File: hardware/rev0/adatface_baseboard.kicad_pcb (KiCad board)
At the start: 4 copper layers, 121.3 x 111.6 mm, 90 parts, among them J1 Conn_01x06_Male, J2 Conn_02x32_Odd_Even, J3 Conn_02x32_Odd_Even, J4 Connector_USB_C_Receptacle_US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, J5 Connector_USB_C_Receptacle_US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, J6 Conn_01x06_Male, J7 Conn_01x26_Male, J8 Conn_01x01_Male, J9 Conn_01x01_Male, U1 PLR135_T8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

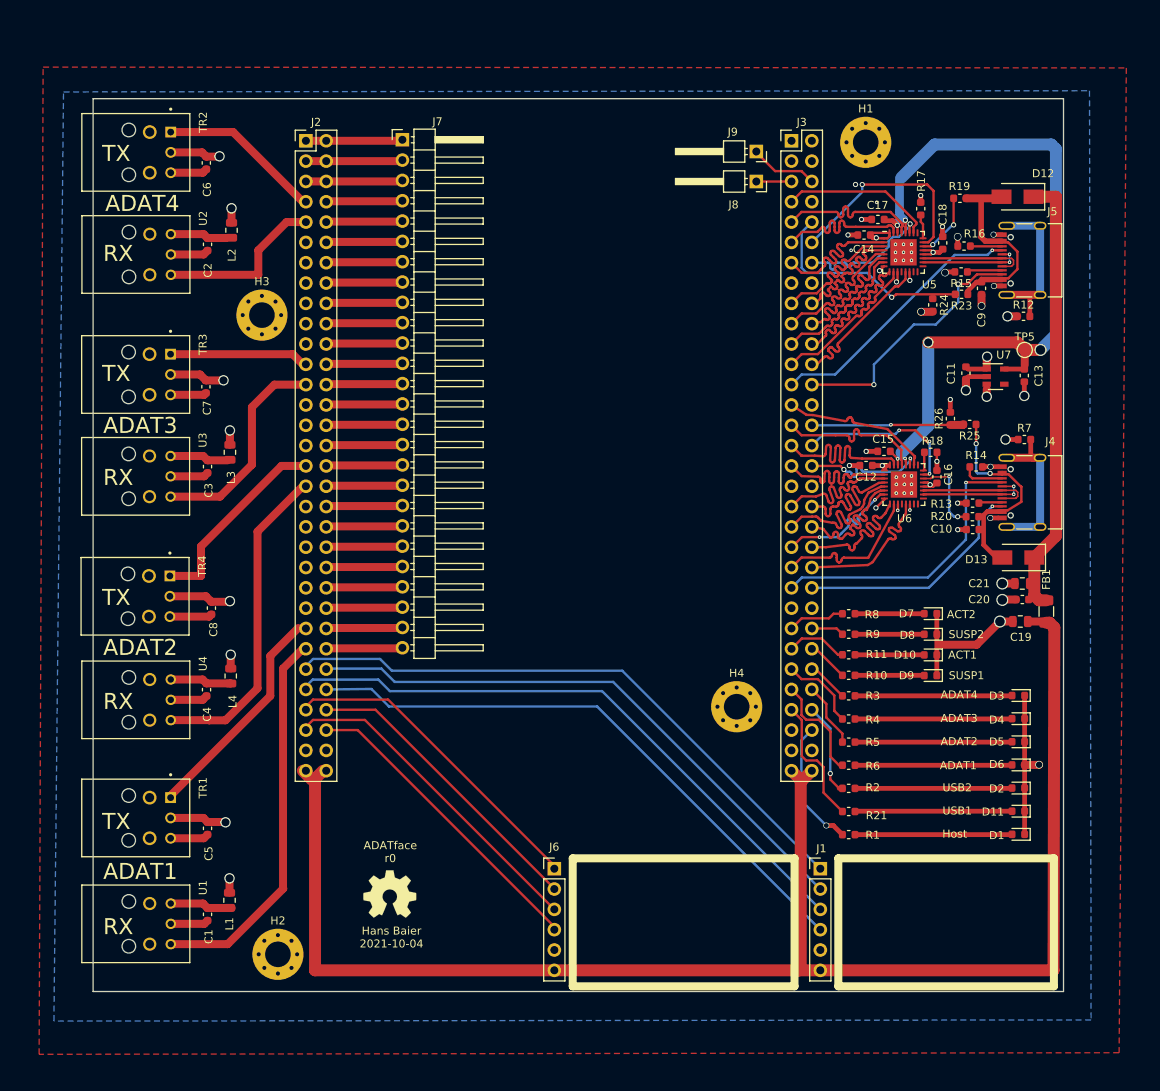
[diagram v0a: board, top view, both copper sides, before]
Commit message: fix hole-hole spacing issues
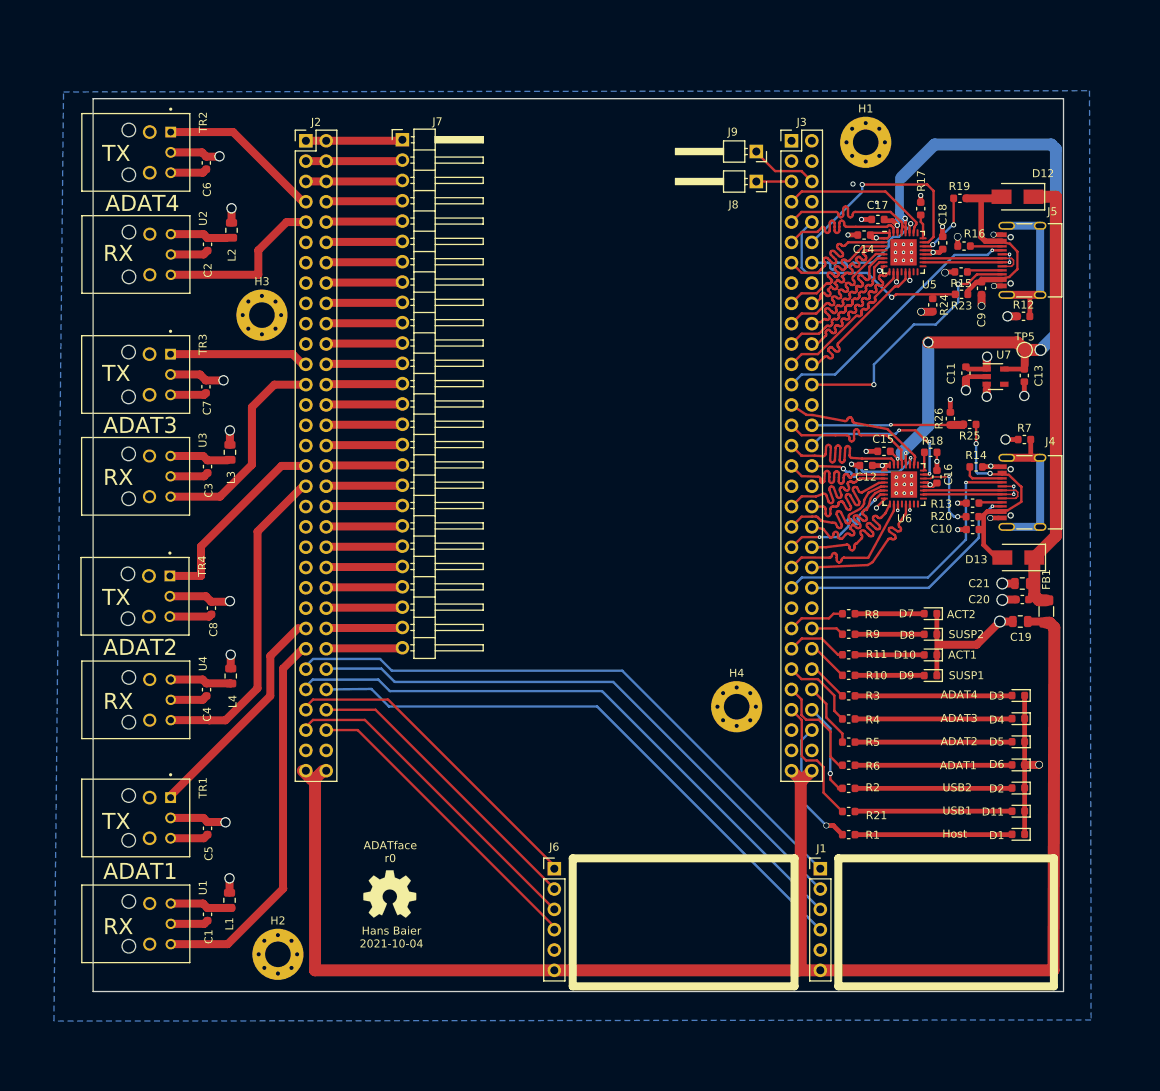
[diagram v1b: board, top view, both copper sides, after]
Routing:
- net +1V8: track 104.1 -> 104.8 mm
- net GND: track 137.8 -> 137.5 mm, vias 47 -> 46
- removed copper zone on F.Cu, net GND

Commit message: fix DRC errors
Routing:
- net /USB1_DIR: track 23.6 -> 18.9 mm
- net GND: track 137.5 -> 141.7 mm
- net /USB1_VBUS: track 34.1 -> 35.8 mm
- net /USB1_D-: track 13.4 -> 14.6 mm
- net /USB2_VBUS: track 36.4 -> 37.5 mm
- net +1V8: track 104.8 -> 105.7 mm
- net /USB2_D-: track 13.4 -> 14.0 mm
- net /USB1_SBU2: track 29.3 -> 29.9 mm

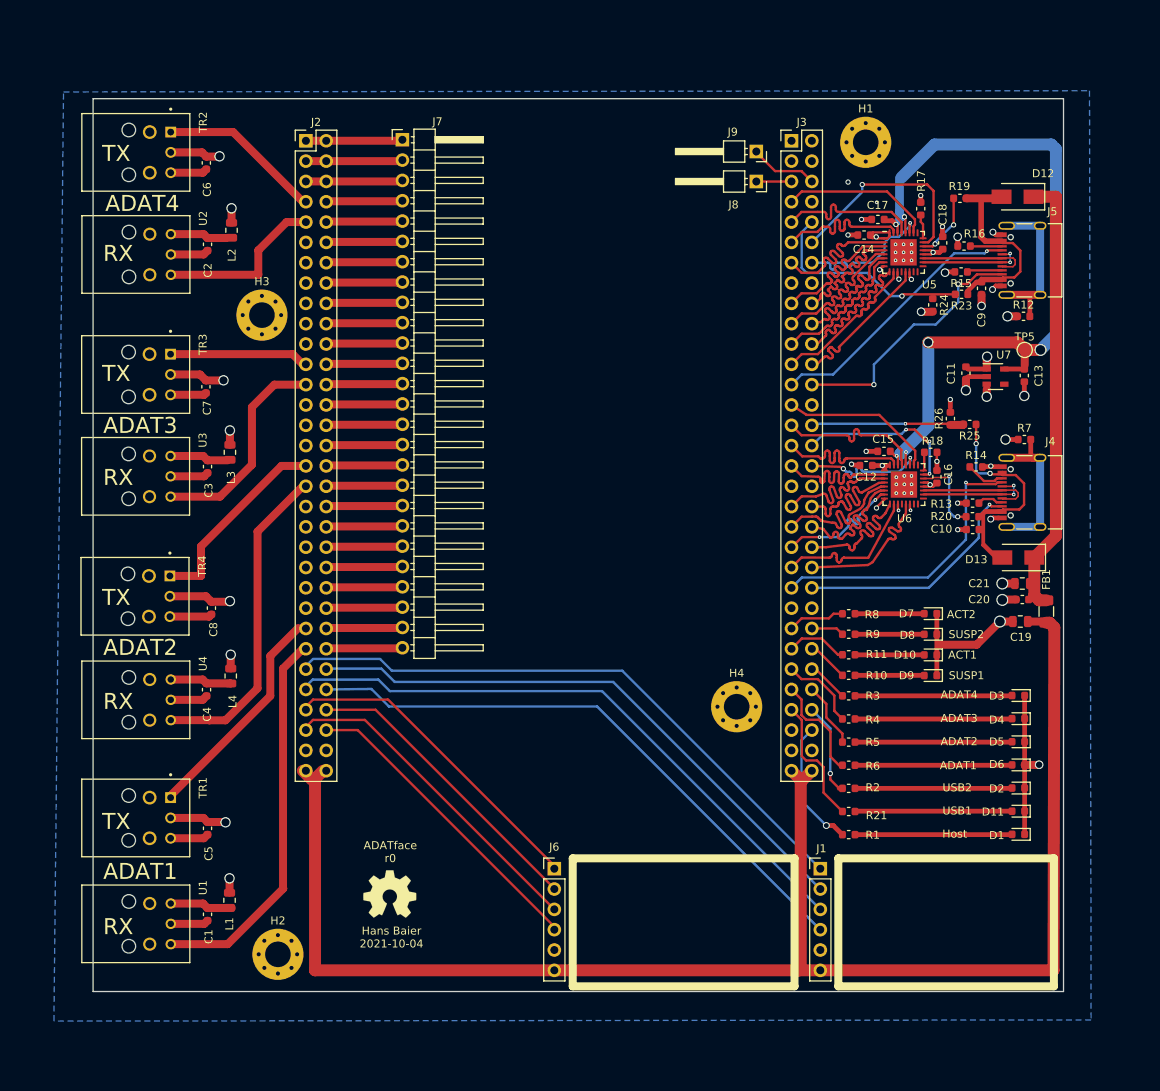
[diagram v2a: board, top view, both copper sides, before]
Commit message: remove 'custom' design rules causing trouble
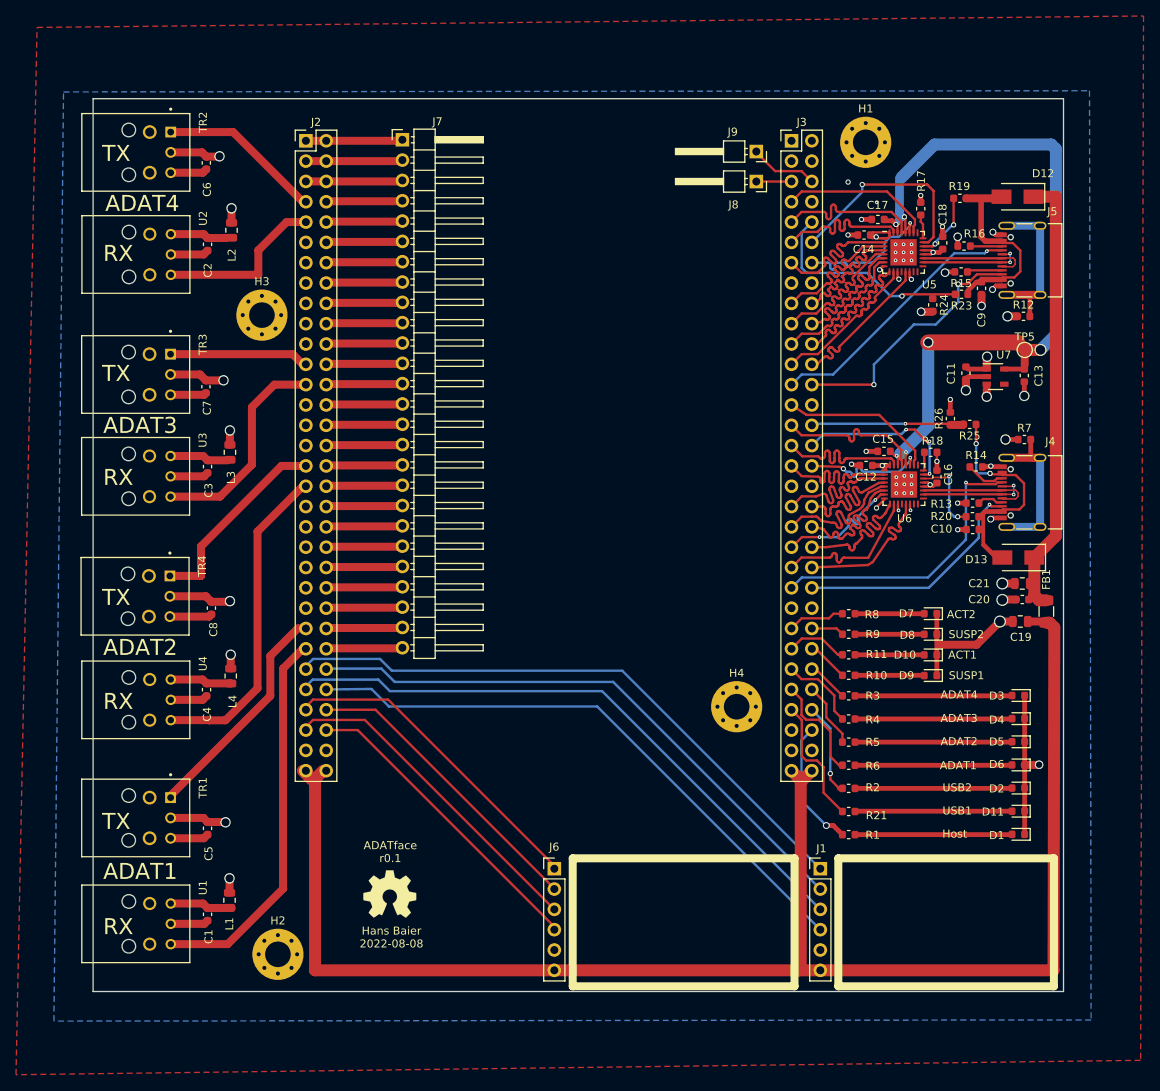
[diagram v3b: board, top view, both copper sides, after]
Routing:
- added copper zone on F.Cu, net GND
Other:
- board text added: "ADATface r0.1"
- board text added: "Hans Baier 2022-08-08"
- board text removed: "ADATface r0"
- board text removed: "Hans Baier 2021-10-04"
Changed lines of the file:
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@@
   (gr_rect (start 101.3 131.6) (end 129.025 147.6) (layer "F.SilkS") (width 1) (fill none))
   (gr_rect (start 41.35 36.65) (end 162.65 148.25) (layer "Edge.Cuts") (width 0.15) (fill none))
-  (gr_text "Hans Baier\n2021-10-04" (at 78.65 141.475) (layer "F.SilkS")
+  (gr_text "Hans Baier\n2022-08-08" (at 78.65 141.475) (layer "F.SilkS")
     (effects (font (size 1 1) (thickness 0.15)))
   )
@@
     (effects (font (size 2 2) (thickness 0.3)))
   )
-  (gr_text "ADATface\nr0" (at 78.5 130.8) (layer "F.SilkS")
+  (gr_text "ADATface\nr0.1" (at 78.5 130.8) (layer "F.SilkS")
     (effects (font (size 1 1) (thickness 0.15)))
   )
@@
   (segment (start 152.35 49.1) (end 152.5 49.25) (width 0.6) (layer "F.Cu") (net 7))
   (segment (start 152.5 53.9) (end 152.5 49.25) (width 0.4) (layer "F.Cu") (net 7))
-  (segment (start 156.859048 67.109048) (end 145.73784 67.109048) (width 1.5) (layer "F.Cu") (net 8))
+  (segment (start 156.859048 67.109048) (end 145.73784 67.109048) (width 2) (layer "F.Cu") (net 8))
   (segment (start 141.795263 81.29) (end 141.95 81.444737) (width 0.3) (layer "F.Cu") (net 8))
   (segment (start 141.95 81.444737) (end 141.95 82.4375) (width 0.3) (layer "F.Cu") (net 8))
@@
   (segment (start 79.445 105.35) (end 79.45 105.355) (width 1) (layer "F.Cu") (net 141))
   (segment (start 71.19 105.35) (end 79.445 105.35) (width 1) (layer "F.Cu") (net 141))
+  (zone (net 1) (net_name "GND") (layer "F.Cu") (hatch edge 0.508)
+    (connect_pads (clearance 0.508))
+    (min_thickness 0.254) (filled_areas_thickness no)
+    (fill yes (thermal_gap 0.508) (thermal_bridge_width 0.508))
+    (polygon
+      (pts
+        (xy 172.29 156.85)
+        (xy 31.71 158.65)
+        (xy 34.34 27.74)
+        (xy 172.65 26.31)
+      )
+    )
+  )
   (zone (net 1) (net_name "GND") (layer "In1.Cu") (hatch edge 0.508)
     (connect_pads (clearance 0.508))

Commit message: baseboard rev0.1: Fix DRC rules with new KiCAD version, length matched USB PHY traces, more ground vias, fix trace spacing, ground headers
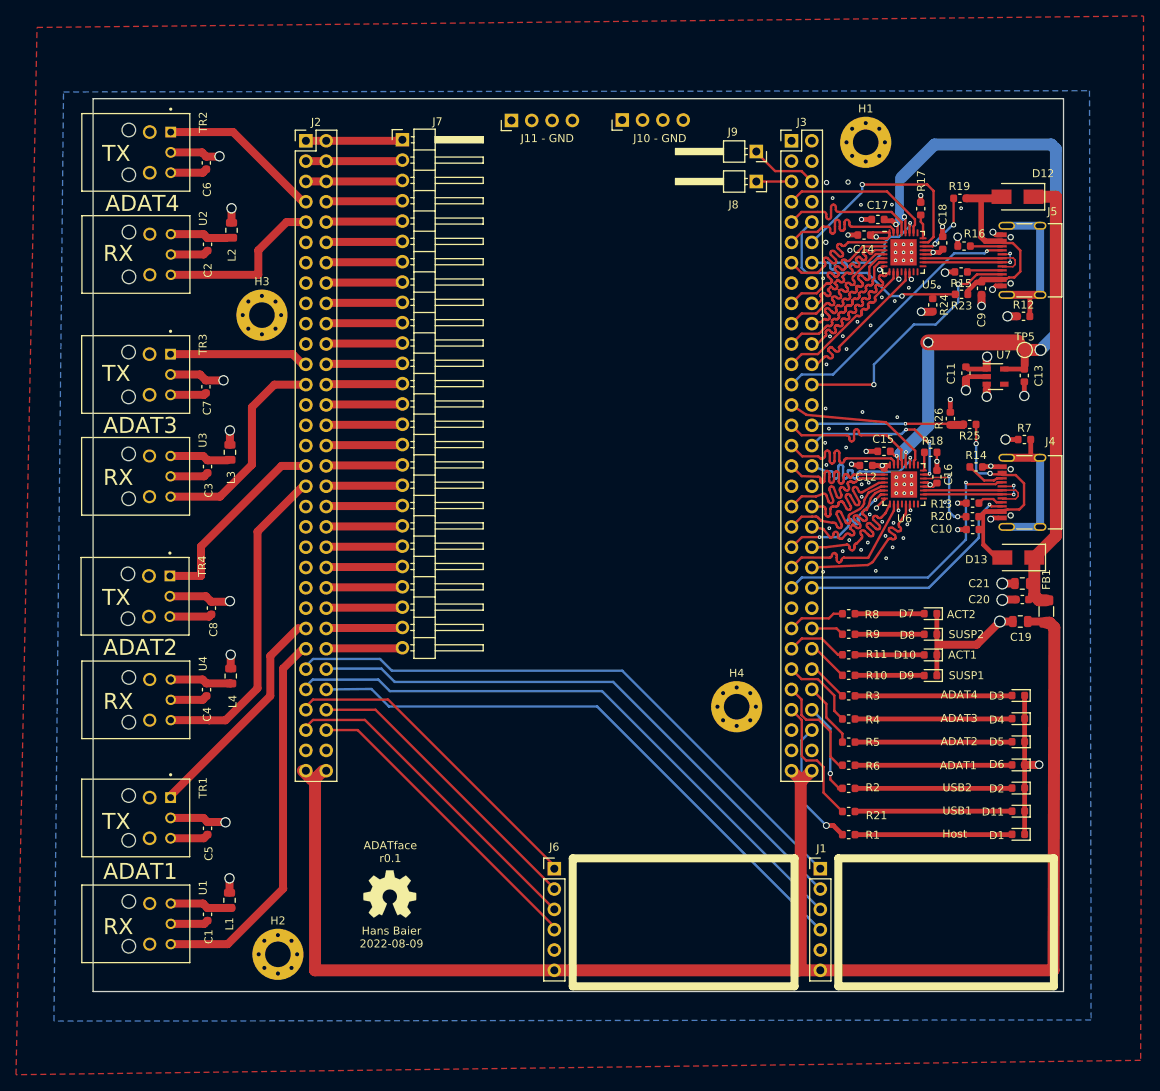
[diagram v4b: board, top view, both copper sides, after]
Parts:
- added J10 - GND: Conn_01x04_Male, Connector_PinHeader_2.54mm:PinHeader_1x04_P2.54mm_Horizontal, F.Cu at (107.5, 39.3)
- added J11 - GND: Conn_01x04_Male, Connector_PinHeader_2.54mm:PinHeader_1x04_P2.54mm_Horizontal, F.Cu at (93.6, 39.4)
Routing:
- net +3V3: track 74.4 -> 84.0 mm
- net /USB1_RESET: track 15.8 -> 20.0 mm, vias 2 -> 1
- net GND: vias 46 -> 91
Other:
- board text added: "Hans Baier 2022-08-09"
- board text removed: "Hans Baier 2022-08-08"
